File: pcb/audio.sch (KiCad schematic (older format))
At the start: 1 part

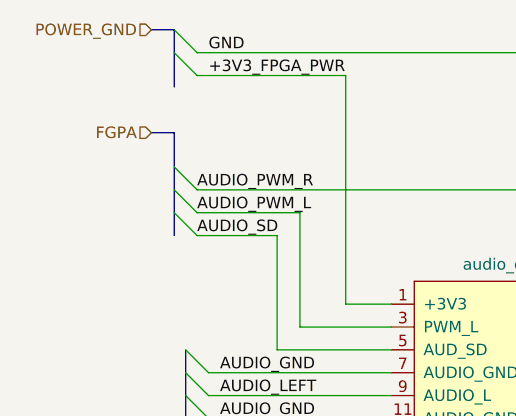
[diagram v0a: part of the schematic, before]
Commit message: bus name typo fixed on audio sheet
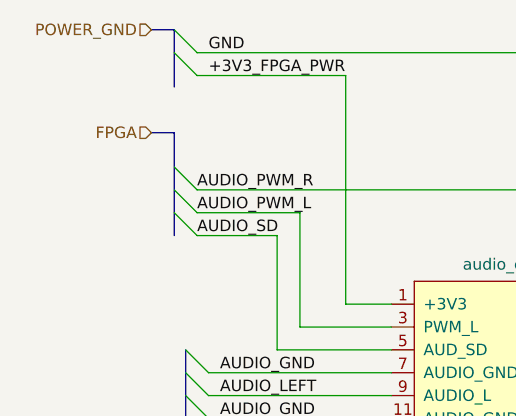
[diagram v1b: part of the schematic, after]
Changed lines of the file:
@@
 AUDIO
 Text HLabel 1350 1350 0    50   Input ~ 0
-FGPA
+FPGA
 Wire Bus Line
 	1350 1350 1450 1350

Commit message: Some work done on the whole project
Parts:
- gave numbers to parts that had none: 1
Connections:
- net AUDIO_PWM_L renamed FPGA_AUD_PWM_L
- net AUDIO_PWM_R renamed FPGA_AUD_PWM_R
- net AUDIO_SD renamed FPGA_AUD_SD
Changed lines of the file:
@@
 $Descr A4 11693 8268
 encoding utf-8
-Sheet 7 11
+Sheet 11 11
 Title "WishMaster 1200"
 Date ""
@@
 	1450 1500 1550 1600
 Wire Wire Line
-	1550 1700 2000 1700
+	1550 1700 2150 1700
 Text Label 1550 1700 0    50   ~ 0
-AUDIO_PWM_L
+FPGA_AUD_PWM_L
 Text Label 1550 1600 0    50   ~ 0
-AUDIO_PWM_R
+FPGA_AUD_PWM_R
 Text HLabel 1350 900  0    50   Input ~ 0
 POWER_GND
 $Comp
-L WM1200:audio_expansion X?
+L WM1200:audio_expansion X5
 U 1 1 5EB21AAB
 P 3000 2700
-F 0 "X?" H 3000 3565 50  0000 C CNN
+F 0 "X5" H 3000 3565 50  0000 C CNN
 F 1 "audio_expansion" H 3000 3474 50  0000 C CNN
 F 2 "" H 2400 2950 50  0001 C CNN
@@
 	1550 1600 4000 1600
 Wire Wire Line
-	2000 1700 2000 2200
+	2150 1700 2150 2200
 Wire Wire Line
-	2000 2200 2400 2200
+	2150 2200 2400 2200
 Entry Wire Line
 	1500 2300 1600 2400
@@
 	1900 2300 2400 2300
 Text Label 1550 1800 0    50   ~ 0
-AUDIO_SD
+FPGA_AUD_SD
 Wire Bus Line
 	1350 900  1450 900
@@
 	1450 1000 1550 1100
 Wire Wire Line
-	1550 1100 2200 1100
+	1550 1100 2300 1100
 Wire Wire Line
-	2200 1100 2200 2100
+	2300 1100 2300 2100
 Wire Wire Line
-	2200 2100 2400 2100
+	2300 2100 2400 2100
 Wire Wire Line
 	3750 2100 3600 2100

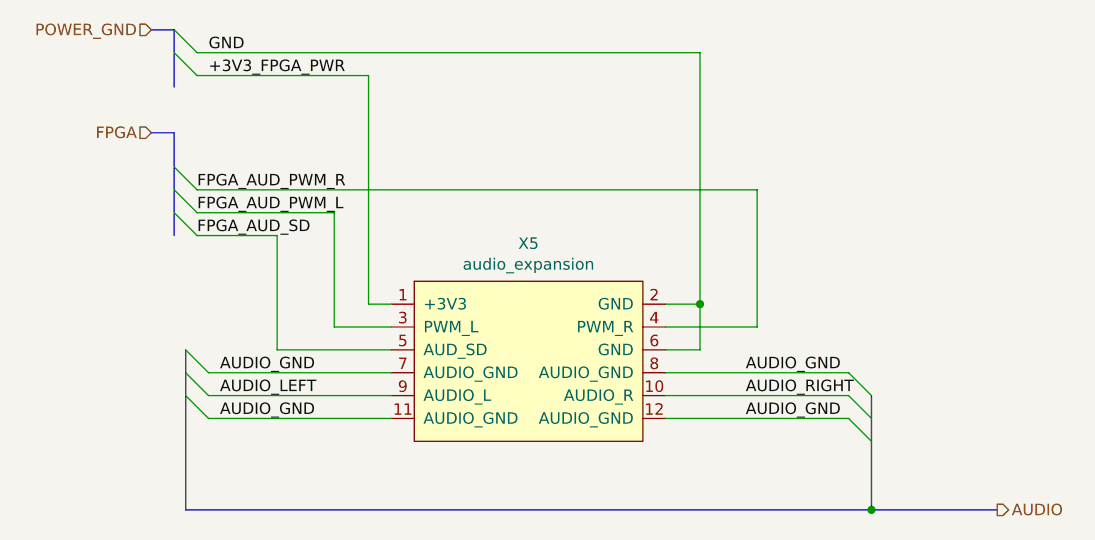
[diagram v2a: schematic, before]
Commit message: ok, we are using global labels now
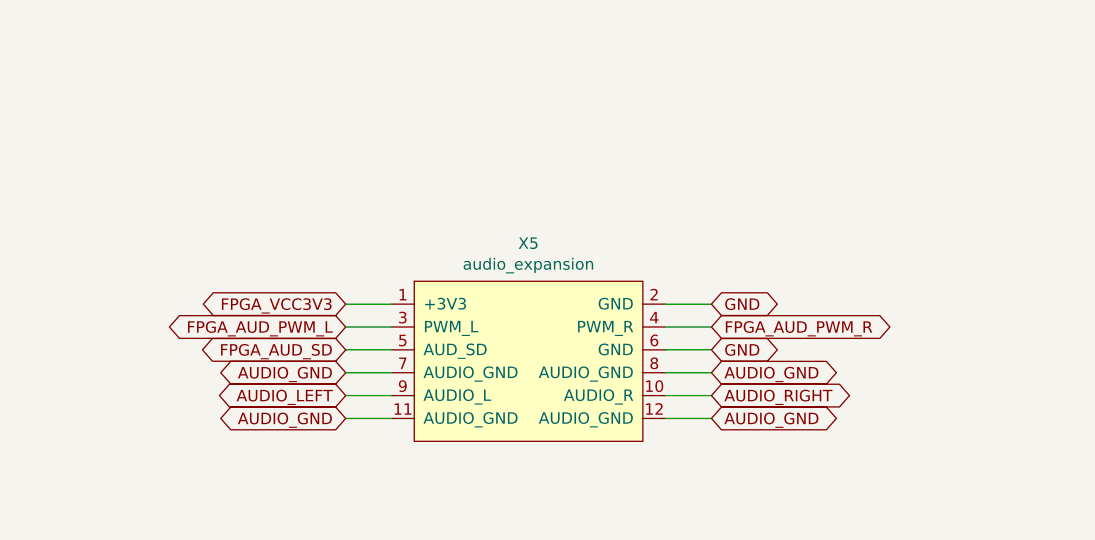
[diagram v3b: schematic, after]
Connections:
- net +3V3_FPGA_PWR renamed FPGA_VCC3V3
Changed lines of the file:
@@
 $Descr A4 11693 8268
 encoding utf-8
-Sheet 11 11
+Sheet 7 11
 Title "WishMaster 1200"
 Date ""
@@
 Comment4 ""
 $EndDescr
-Text HLabel 5050 3000 2    50   Output ~ 0
-AUDIO
-Text HLabel 1350 1350 0    50   Input ~ 0
-FPGA
-Wire Bus Line
-	1350 1350 1450 1350
-Entry Wire Line
-	1450 1600 1550 1700
-Entry Wire Line
-	1450 1500 1550 1600
-Wire Wire Line
-	1550 1700 2150 1700
-Text Label 1550 1700 0    50   ~ 0
-FPGA_AUD_PWM_L
-Text Label 1550 1600 0    50   ~ 0
-FPGA_AUD_PWM_R
-Text HLabel 1350 900  0    50   Input ~ 0
-POWER_GND
 $Comp
 L WM1200:audio_expansion X5
@@
 	1    0    0    -1
 $EndComp
-Wire Bus Line
-	1500 3000 4500 3000
-Connection ~ 4500 3000
-Wire Bus Line
-	4500 3000 5050 3000
 Wire Wire Line
-	4000 1600 4000 2200
+	2400 2500 2200 2500
 Wire Wire Line
-	4000 2200 3600 2200
+	2200 2600 2400 2600
 Wire Wire Line
-	1550 1600 4000 1600
+	3600 2400 3800 2400
 Wire Wire Line
-	2150 1700 2150 2200
+	3800 2500 3600 2500
 Wire Wire Line
-	2150 2200 2400 2200
-Entry Wire Line
-	1500 2300 1600 2400
-Entry Wire Line
-	1500 2400 1600 2500
-Entry Wire Line
-	1500 2500 1600 2600
-Entry Wire Line
-	4400 2400 4500 2500
-Entry Wire Line
-	4400 2500 4500 2600
-Entry Wire Line
-	4400 2600 4500 2700
+	3600 2600 3800 2600
+Text GLabel 3800 2100 2    50   BiDi ~ 0
+GND
+Text GLabel 2200 2100 0    50   BiDi ~ 0
+FPGA_VCC3V3
+Text GLabel 3800 2200 2    50   BiDi ~ 0
+FPGA_AUD_PWM_R
+Text GLabel 2200 2200 0    50   BiDi ~ 0
+FPGA_AUD_PWM_L
+Text GLabel 2200 2300 0    50   BiDi ~ 0
+FPGA_AUD_SD
+Text GLabel 2200 2400 0    50   BiDi ~ 0
+AUDIO_GND
+Text GLabel 2200 2500 0    50   BiDi ~ 0
+AUDIO_LEFT
+Text GLabel 2200 2600 0    50   BiDi ~ 0
+AUDIO_GND
+Text GLabel 3800 2400 2    50   BiDi ~ 0
+AUDIO_GND
+Text GLabel 3800 2600 2    50   BiDi ~ 0
+AUDIO_GND
+Text GLabel 3800 2500 2    50   BiDi ~ 0
+AUDIO_RIGHT
 Wire Wire Line
-	1600 2400 2400 2400
+	2200 2400 2400 2400
+Text GLabel 3800 2300 2    50   BiDi ~ 0
+GND
 Wire Wire Line
-	2400 2500 1600 2500
+	2200 2100 2400 2100
 Wire Wire Line
-	1600 2600 2400 2600
+	2400 2200 2200 2200
 Wire Wire Line
-	3600 2400 4400 2400
+	2200 2300 2400 2300
 Wire Wire Line
-	4400 2500 3600 2500
+	3600 2100 3800 2100
 Wire Wire Line
-	3600 2600 4400 2600
-Entry Wire Line
-	1450 1700 1550 1800
+	3800 2200 3600 2200
 Wire Wire Line
-	1550 1800 1900 1800
-Wire Wire Line
-	1900 1800 1900 2300
-Wire Wire Line
-	1900 2300 2400 2300
-Text Label 1550 1800 0    50   ~ 0
-FPGA_AUD_SD
-Wire Bus Line
-	1350 900  1450 900
-Entry Wire Line
-	1450 900  1550 1000
-Entry Wire Line
-	1450 1000 1550 1100
-Wire Wire Line
-	1550 1100 2300 1100
-Wire Wire Line
-	2300 1100 2300 2100
-Wire Wire Line
-	2300 2100 2400 2100
-Wire Wire Line
-	3750 2100 3600 2100
-Wire Wire Line
-	3750 2100 3750 2300
-Wire Wire Line
-	3750 2300 3600 2300
-Connection ~ 3750 2100
-Wire Wire Line
-	1550 1000 3750 1000
-Wire Wire Line
-	3750 1000 3750 2100
-Text Label 1600 1100 0    50   ~ 0
-+3V3_FPGA_PWR
-Text Label 1600 1000 0    50   ~ 0
-GND
-Text Label 1650 2400 0    50   ~ 0
-AUDIO_GND
-Text Label 1650 2600 0    50   ~ 0
-AUDIO_GND
-Text Label 3950 2600 0    50   ~ 0
-AUDIO_GND
-Text Label 3950 2400 0    50   ~ 0
-AUDIO_GND
-Text Label 1650 2500 0    50   ~ 0
-AUDIO_LEFT
-Text Label 3950 2500 0    50   ~ 0
-AUDIO_RIGHT
-Wire Bus Line
-	1450 900  1450 1150
-Wire Bus Line
-	1500 2300 1500 3000
-Wire Bus Line
-	4500 2500 4500 3000
-Wire Bus Line
-	1450 1350 1450 1800
+	3600 2300 3800 2300
 $EndSCHEMATC

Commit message: fpga-side gpio connector added
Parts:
- renumbered X5 to X2
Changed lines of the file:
@@
 $EndDescr
 $Comp
-L WM1200:audio_expansion X5
+L WM1200:audio_expansion X2
 U 1 1 5EB21AAB
 P 3000 2700
-F 0 "X5" H 3000 3565 50  0000 C CNN
+F 0 "X2" H 3000 3565 50  0000 C CNN
 F 1 "audio_expansion" H 3000 3474 50  0000 C CNN
 F 2 "" H 2400 2950 50  0001 C CNN

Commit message: more footprints assigned
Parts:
- renumbered X2 to X1
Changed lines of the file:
@@
 $EndDescr
 $Comp
-L WM1200:audio_expansion X2
+L WM1200:audio_expansion X1
 U 1 1 5EB21AAB
 P 3000 2700
-F 0 "X2" H 3000 3565 50  0000 C CNN
+F 0 "X1" H 3000 3565 50  0000 C CNN
 F 1 "audio_expansion" H 3000 3474 50  0000 C CNN
 F 2 "" H 2400 2950 50  0001 C CNN

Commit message: More footprints assigned
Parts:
- X1: footprint (none) -> Connector_PinHeader_2.54mm:PinHeader_2x06_P2.54mm_Vertical
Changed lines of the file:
@@
 F 0 "X1" H 3000 3565 50  0000 C CNN
 F 1 "audio_expansion" H 3000 3474 50  0000 C CNN
-F 2 "" H 2400 2950 50  0001 C CNN
+F 2 "Connector_PinHeader_2.54mm:PinHeader_2x06_P2.54mm_Vertical" H 2400 2950 50  0001 C CNN
 F 3 "" H 2400 2950 50  0001 C CNN
 	1    3000 2700
